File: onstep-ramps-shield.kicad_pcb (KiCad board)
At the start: 2 copper layers, 120.7 x 64.8 mm, 24 parts

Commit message: WIP - Routing
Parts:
- added REF**: Pololu_Breakout-16_15.2x20.3mm, Module:Pololu_Breakout-16_15.2x20.3mm, F.Cu at (123.2, 104.1)
- moved BZ1 49.4 mm to (218.4, 104.1)
- moved RA1 44.5 mm to (233.7, 111.8)
- moved BME280 31.8 mm to (203.2, 99.1), turned to 90 degrees
- moved FOC1 31.8 mm to (233.7, 66.0)
- moved FOC2 31.8 mm to (233.7, 81.3)
- moved DS3231 27.9 mm to (203.2, 69.8), turned to 90 degrees
- moved DEC1 14.0 mm to (233.7, 96.5)
- moved J_SERV1 3.81 mm to (139.7, 114.3)
- moved J_SERV2 2.54 mm to (142.2, 114.3)
- moved J_RET1 1.80 mm to (247.7, 110.5)
- moved J_PEC1 1.80 mm to (247.7, 95.2)
- moved J_SERV3 1.27 mm to (144.8, 114.3)
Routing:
- net E0_2B: track 0.00 -> 109.9 mm
- net E0_2A: track 0.00 -> 108.5 mm
- net E0_1A: track 0.00 -> 102.4 mm
- net E0_1B: track 0.00 -> 101.9 mm
- net E1_2B: track 0.00 -> 90.0 mm
- net E1_2A: track 0.00 -> 88.6 mm
- net E1_1A: track 0.00 -> 82.1 mm
- net E1_1B: track 0.00 -> 81.9 mm
- net (no net): track 0.00 -> 20.3 mm
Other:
- board size 120.7 x 64.8 mm -> 120.7 x 67.3 mm

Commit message: Routing
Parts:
- removed the REF** at (123.2, 104.1)
- added REF**: OSHW-Logo2_7.3x6mm_SilkScreen, Symbol:OSHW-Logo2_7.3x6mm_SilkScreen, F.Cu at (134.6, 111.8)
- moved R1 78.0 mm to (151.1, 115.6)
- moved BZ1 62.9 mm to (174.0, 59.7), turned to 0 degrees
- moved DS3231 16.9 mm to (207.0, 53.3)
- moved BME280 14.5 mm to (207.0, 113.0)
- moved J_I2C1 7.62 mm to (193.0, 68.6), turned to 0 degrees
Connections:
- net Net-(BZ1-Pad1) renamed BUZZER
- BME280 pad 1: GND -> SPI_GND
- BME280 pad 3: VCC -> SPI_VCC
- BZ1 pad 2: Net-(BZ1-Pad2) -> GND
- DS3231 pad 1: GND -> I2C_GND
- DS3231 pad 2: VCC -> I2C_VCC
- J_AUX1 pad 1: VCC -> (no net)
- J_AUX1 pad 2: GND -> (no net)
- J_AUX2 pad 1: VCC -> (no net)
- J_AUX2 pad 2: GND -> (no net)
- J_AUX3 pad 1: VCC -> SPI_VCC
- J_AUX3 pad 7: GND -> SPI_GND
- J_I2C1 pad 1: VCC -> I2C_VCC
- J_I2C1 pad 2: GND -> I2C_GND
- J_SERV1 pad 1: GND -> (no net)
- J_SERV1 pad 2: VCC -> (no net)
- J_SERV2 pad 1: GND -> (no net)
- J_SERV2 pad 2: VCC -> (no net)
- J_SERV3 pad 1: GND -> (no net)
- J_SERV3 pad 2: VCC -> (no net)
- J_SERV4 pad 1: Net-(BZ1-Pad2) -> (no net)
- J_SERV4 pad 2: VCC -> (no net)
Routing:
- net Y_2B: track 0.00 -> 121.4 mm, vias 0 -> 1
- net X_2B: track 0.00 -> 120.4 mm, vias 0 -> 2
- net X_2A: track 0.00 -> 120.0 mm, vias 0 -> 1
- net X_1A: track 0.00 -> 114.5 mm, vias 0 -> 1
- net X_1B: track 0.00 -> 114.0 mm, vias 0 -> 1
- net Y_2A: track 0.00 -> 110.8 mm, vias 0 -> 1
- net Y_1A: track 0.00 -> 107.5 mm, vias 0 -> 1
- net Net-(J_RET1-PadS): track 0.00 -> 99.8 mm
- net GND: track 0.00 -> 99.1 mm
- net PEC: track 0.00 -> 96.8 mm, vias 0 -> 2
- net BUZZER: track 0.00 -> 94.4 mm
- net Y_1B: track 0.00 -> 93.3 mm, vias 0 -> 1
- net VCC: track 0.00 -> 71.2 mm
- net CS_BME280: track 0.00 -> 33.7 mm
- net SDA: track 0.00 -> 33.6 mm
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
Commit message: Routing
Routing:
- net Net-(J_RET1-PadS): track 99.8 -> 98.7 mm

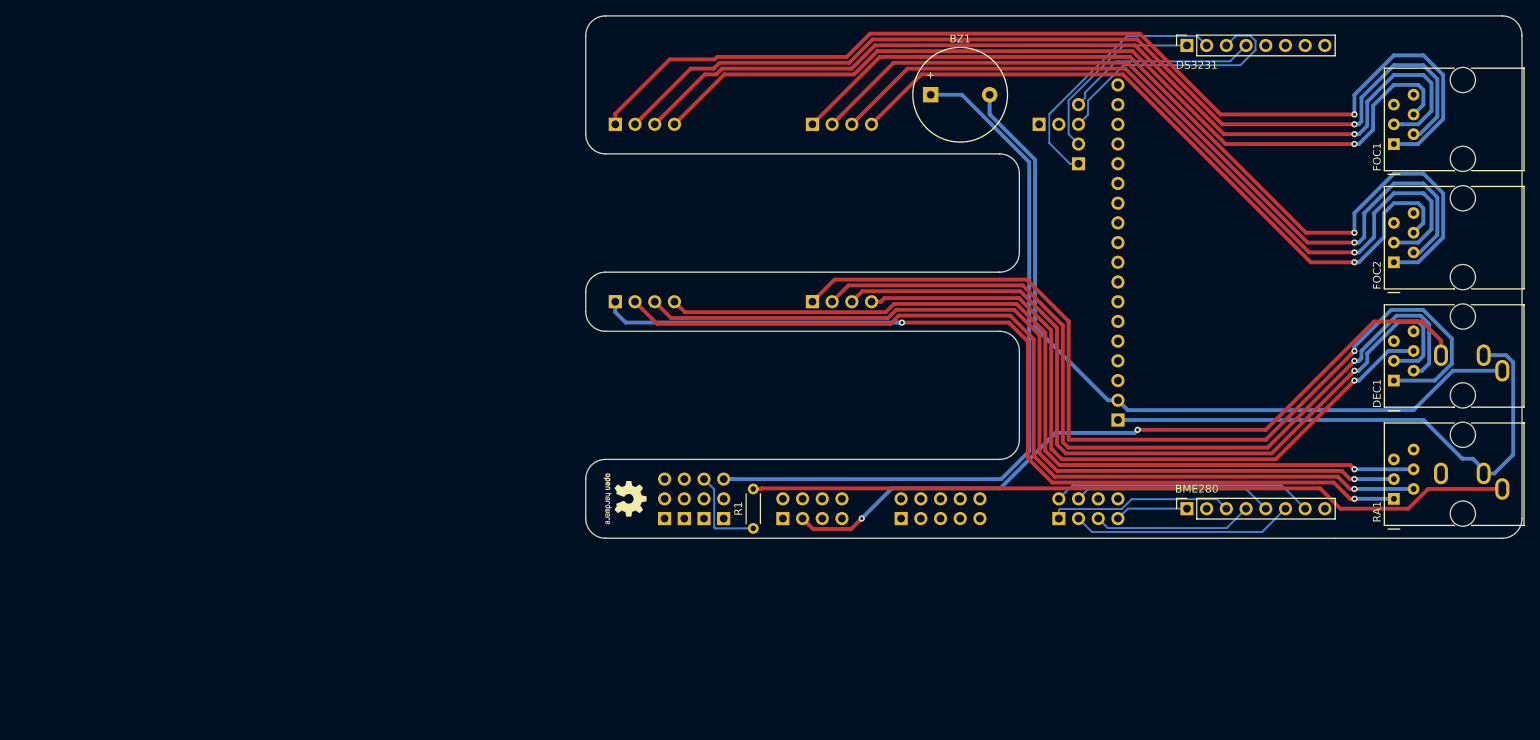
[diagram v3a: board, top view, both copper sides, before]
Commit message: Include HC05
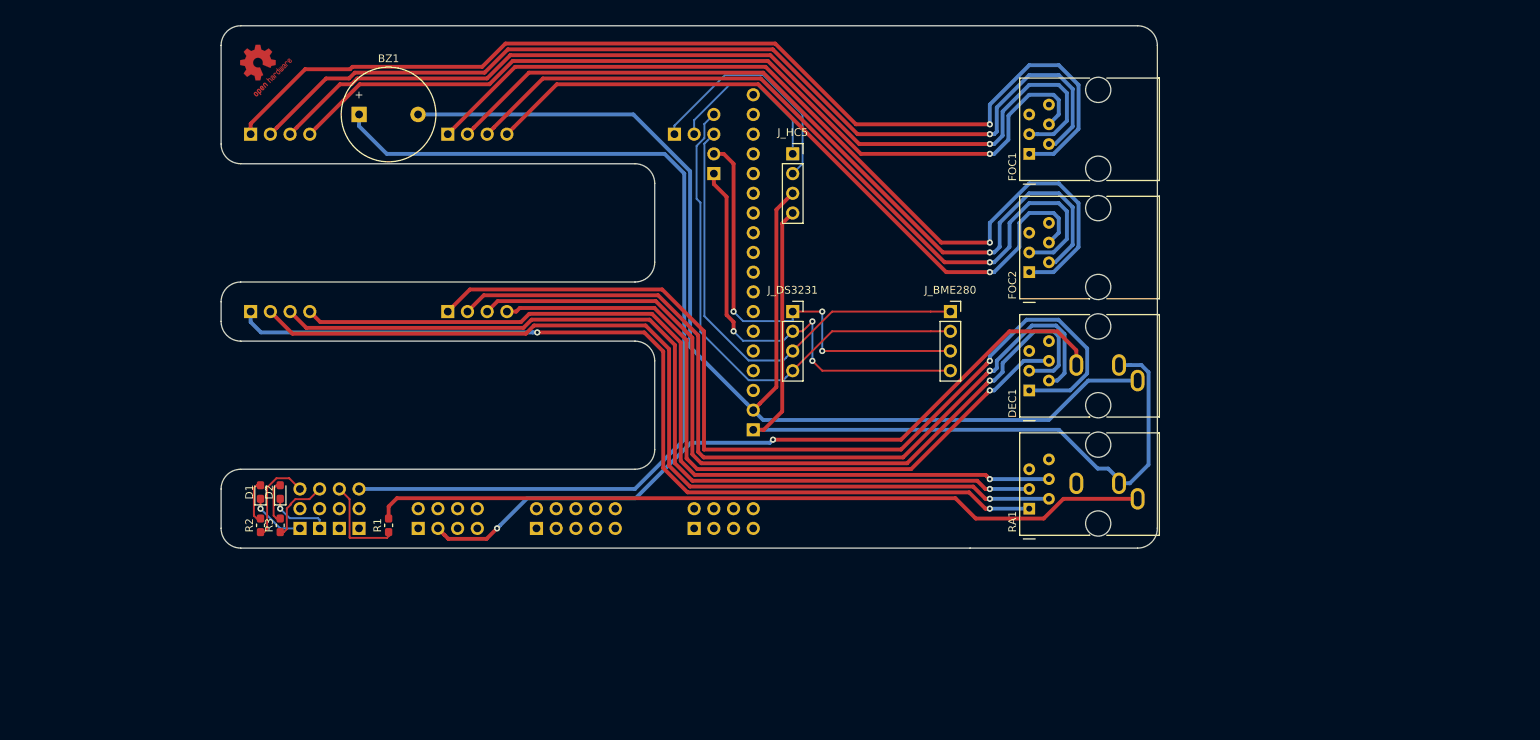
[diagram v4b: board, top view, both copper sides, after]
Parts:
- removed BME280, DS3231: Conn_01x08, Connector_PinSocket_2.54mm:PinSocket_1x08_P2.54mm_Vertical
- removed the REF** at (134.6, 111.8)
- added D1: LED, LED_SMD:LED_0603_1608Metric_Pad1.05x0.95mm_HandSolder, F.Cu at (87.6, 110.9)
- added D2: LED, LED_SMD:LED_0603_1608Metric_Pad1.05x0.95mm_HandSolder, F.Cu at (90.2, 110.9)
- added J_BME280: Conn_01x04_Female, Connector_PinSocket_2.54mm:PinSocket_1x04_P2.54mm_Vertical, F.Cu at (176.5, 87.6)
- added J_DS3231: Conn_01x04_Female, Connector_PinSocket_2.54mm:PinSocket_1x04_P2.54mm_Vertical, F.Cu at (156.2, 87.6)
- added J_HC5: Conn_01x04_Female, Connector_PinSocket_2.54mm:PinSocket_1x04_P2.54mm_Vertical, F.Cu at (156.2, 67.3)
- added R2: 350, Resistor_SMD:R_0603_1608Metric_Pad1.05x0.95mm_HandSolder, F.Cu at (87.6, 115.2)
- added R3: 350, Resistor_SMD:R_0603_1608Metric_Pad1.05x0.95mm_HandSolder, F.Cu at (90.2, 115.2)
- added REF**: OSHW-Logo2_7.3x6mm_Copper, Symbol:OSHW-Logo2_7.3x6mm_Copper, F.Cu at (87.6, 55.9)
- R1: footprint Resistor_THT:R_Axial_DIN0204_L3.6mm_D1.6mm_P5.08mm_Horizontal -> Resistor_SMD:R_0603_1608Metric_Pad1.05x0.95mm_HandSolder
- moved BZ1 73.7 mm to (100.3, 62.2)
- moved DEC1 47.0 mm to (186.7, 97.8)
- moved FOC1 47.0 mm to (186.7, 67.3)
- moved FOC2 47.0 mm to (186.7, 82.5)
- moved J_AUX2 47.0 mm to (123.2, 115.6)
- moved J_AUX3 47.0 mm to (143.5, 115.6)
- moved J_AUX4 47.0 mm to (151.1, 102.9)
- moved J_PEC1 47.0 mm to (200.7, 96.5)
- moved J_RET1 47.0 mm to (200.7, 111.8)
- moved J_SER1 47.0 mm to (141.0, 64.8)
- moved J_SERV2 47.0 mm to (95.2, 115.6)
- moved RA1 47.0 mm to (186.7, 113.0)
- moved J_AUX1 47.0 mm to (108.0, 115.6)
- moved J_DEC1 47.0 mm to (111.8, 87.6)
- moved J_FOC1 47.0 mm to (86.4, 64.8)
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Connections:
- net BUZZER renamed BUZZER1
- net RETICULE_LED renamed RETICULE_LED1
- J_AUX1 pad 3: PEC -> (no net)
- J_AUX1 pad 5: (no net) -> PEC1
- J_AUX3 pad 1: SPI_VCC -> (no net)
- J_AUX3 pad 2: CS_BME280 -> (no net)
- J_AUX3 pad 3: SDI -> (no net)
- J_AUX3 pad 4: SDO -> (no net)
- J_AUX3 pad 5: SCK -> (no net)
- J_AUX3 pad 7: SPI_GND -> (no net)
- J_I2C1 pad 1: I2C_VCC -> VCC_I2C1
- J_I2C1 pad 2: I2C_GND -> GND_I2C1
- J_I2C1 pad 3: SDA -> I2C_SDA
- J_I2C1 pad 4: SCL -> I2C_SCL
- J_PEC1 pad R: PEC -> PEC1
- J_SER1 pad 1: (no net) -> RX1
- J_SER1 pad 2: (no net) -> TX1
- J_SERV1 pad 1: (no net) -> GND_SERV1
- J_SERV1 pad 3: (no net) -> STATUS_LED1
- J_SERV2 pad 1: (no net) -> GND_SERV2
- J_SERV2 pad 3: (no net) -> STATUS_LED2
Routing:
- net PEC1: track 0.00 -> 96.8 mm, vias 0 -> 2
- net PEC: track 96.8 -> 0.00 mm, vias 2 -> 0
- net I2C_SCL: track 0.00 -> 66.5 mm
- net I2C_SDA: track 0.00 -> 60.6 mm
- net GND_I2C1: track 0.00 -> 56.8 mm, vias 0 -> 3
- net VCC_I2C1: track 0.00 -> 56.5 mm, vias 0 -> 3
- net GND: track 99.1 -> 154.5 mm
- net CS_BME280: track 33.7 -> 0.00 mm
- net SDA: track 33.6 -> 0.00 mm
- net I2C_VCC: track 33.6 -> 0.00 mm
- net VCC: track 71.2 -> 102.0 mm
- net RX1: track 0.00 -> 30.6 mm
- net BUZZER1: track 94.4 -> 124.8 mm
- net SDI: track 28.6 -> 0.00 mm
- net SDO: track 25.7 -> 0.00 mm
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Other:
- board size 120.7 x 67.3 mm -> 120.6 x 67.3 mm

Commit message: Measured distances
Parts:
- added REF**: Pololu_Breakout-16_15.2x20.3mm, Module:Pololu_Breakout-16_15.2x20.3mm, F.Cu at (83.8, 82.5)
- added REF**: Pololu_Breakout-16_15.2x20.3mm, Module:Pololu_Breakout-16_15.2x20.3mm, F.Cu at (83.8, 105.4)
- moved BZ1 83.6 mm to (58.4, 134.6)
- moved J_FOC1 7.62 mm to (94.0, 64.8)
- moved J_RA1 6.35 mm to (92.7, 87.6)
- moved J_I2C1 3.81 mm to (142.2, 69.8)
- moved J_SER1 3.81 mm to (137.2, 64.8)
- moved D1 2.54 mm to (90.2, 110.9)
- moved J_AUX2 2.54 mm to (125.7, 115.6)
- moved J_SERV1 2.54 mm to (95.2, 115.6)
- moved J_SERV2 2.54 mm to (97.8, 115.6)
- moved J_SERV4 2.54 mm to (102.9, 115.6)
- moved R1 2.54 mm to (106.7, 115.2)
- moved R2 2.54 mm to (90.2, 115.2)
- moved D2 2.54 mm to (92.7, 110.9)
- moved J_AUX1 2.54 mm to (110.5, 115.6)
- moved J_SERV3 2.54 mm to (100.3, 115.6)
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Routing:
- net BUZZER1: track 124.8 -> 0.00 mm
- net Net-(J_RET1-PadS): track 100.7 -> 0.00 mm
- net PEC1: track 96.8 -> 0.00 mm, vias 2 -> 0
- net GND: track 154.5 -> 82.2 mm
- net I2C_SCL: track 66.5 -> 22.4 mm
- net I2C_SDA: track 60.6 -> 22.4 mm
- net GND_I2C1: track 56.8 -> 25.4 mm, vias 3 -> 2
- net RX1: track 30.6 -> 0.00 mm
- net VCC_I2C1: track 56.5 -> 26.5 mm, vias 3 -> 2
- net TX1: track 22.6 -> 0.00 mm
- net RETICULE_LED1: track 12.5 -> 0.00 mm
- net E0_1A: track 123.6 -> 116.0 mm
- net E0_2B: track 135.7 -> 128.1 mm
- net E0_2A: track 127.0 -> 119.4 mm
- net E0_1B: track 114.3 -> 106.7 mm
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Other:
- outline, holes or cut-outs redrawn

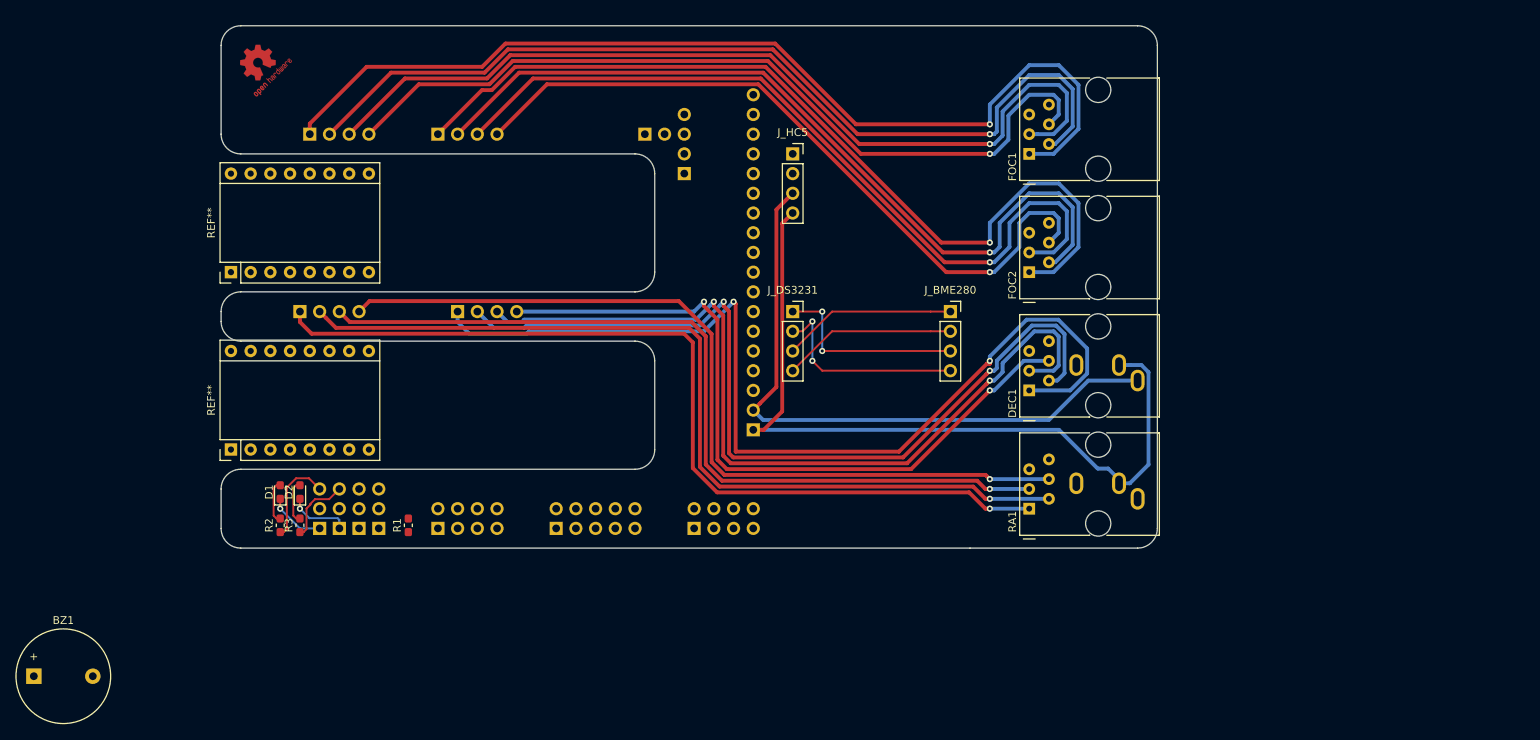
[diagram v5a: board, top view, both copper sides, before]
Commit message: Reorder components
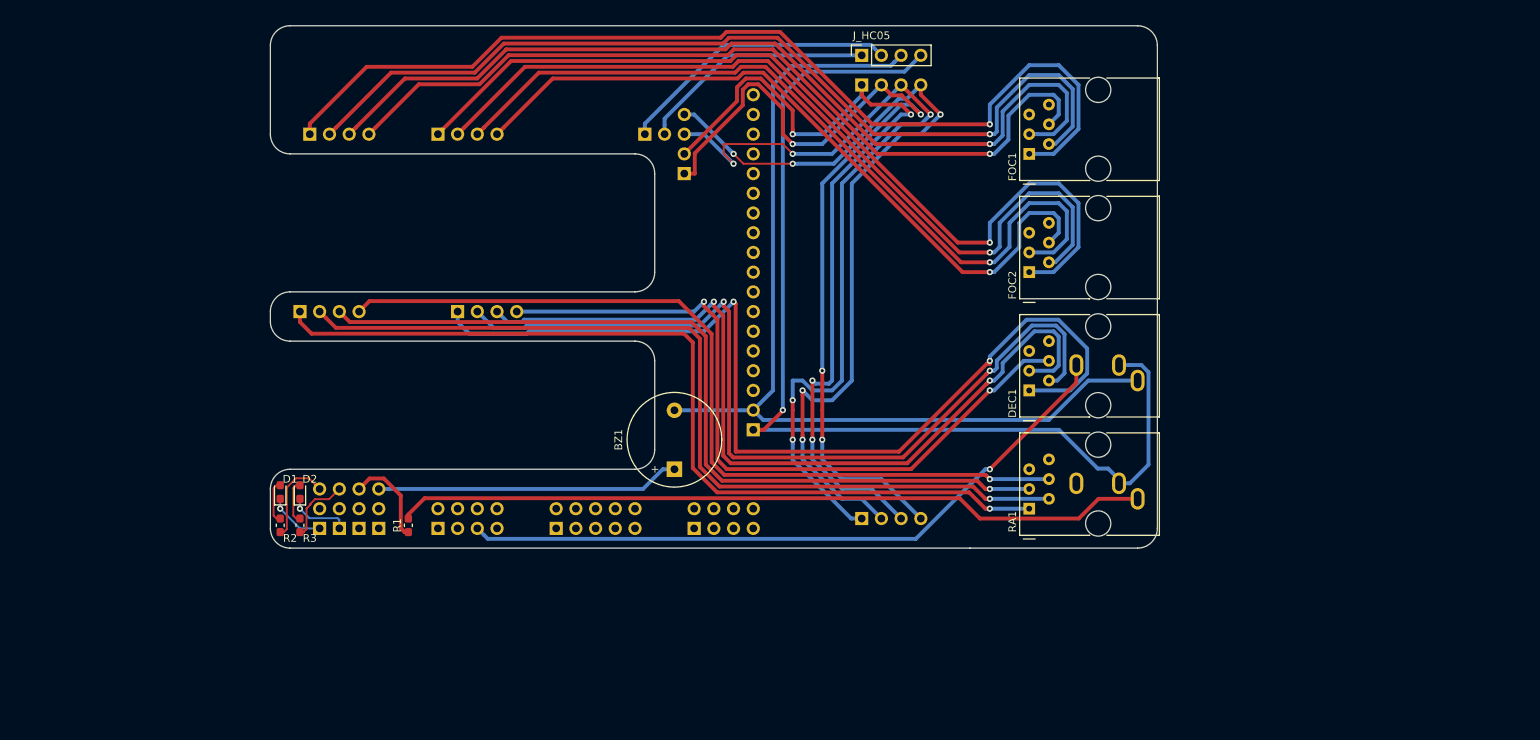
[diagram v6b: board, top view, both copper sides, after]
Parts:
- removed REF** (x2): Pololu_Breakout-16_15.2x20.3mm, Module:Pololu_Breakout-16_15.2x20.3mm
- removed REF**: OSHW-Logo2_7.3x6mm_Copper, Symbol:OSHW-Logo2_7.3x6mm_Copper
- J_BME280, J_DS3231: moved to B.Cu
- moved BZ1 86.8 mm to (141.0, 108.0), turned to 90 degrees
- moved J_DS3231 30.5 mm to (165.1, 58.4), turned to 270 degrees
- moved J_BME280 29.0 mm to (165.1, 114.3), turned to 270 degrees
- moved J_HC05 15.5 mm to (165.1, 54.6), turned to 90 degrees
- renumbered J_HC5 to J_HC05
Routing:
- net Net-(J_RET1-PadS): track 0.00 -> 97.5 mm
- net I2C_SDA: track 22.4 -> 113.6 mm, vias 0 -> 5
- net I2C_SCL: track 22.4 -> 112.8 mm, vias 0 -> 5
- net VCC_I2C1: track 26.5 -> 116.6 mm, vias 2 -> 4
- net PEC1: track 0.00 -> 88.4 mm, vias 0 -> 1
- net GND_I2C1: track 25.4 -> 111.7 mm, vias 2 -> 4
- net GND: track 82.2 -> 123.4 mm
- net BUZZER1: track 0.00 -> 39.2 mm
- net RX1: track 0.00 -> 36.6 mm
- net VCC: track 102.0 -> 136.5 mm, vias 0 -> 1
- net TX1: track 0.00 -> 30.8 mm
- net RETICULE_LED1: track 0.00 -> 12.2 mm
- net E1_1B: track 94.0 -> 95.2 mm
- net E1_2A: track 106.7 -> 107.9 mm
- net E1_1A: track 103.3 -> 104.6 mm
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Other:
- board size 120.6 x 67.3 mm -> 114.3 x 67.3 mm
